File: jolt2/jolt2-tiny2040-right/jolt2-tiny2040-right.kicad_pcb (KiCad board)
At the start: 2 copper layers, 151 x 98 mm, 34 parts, among them J1 Conn_01x02_Pin, J10 Conn_01x02_Pin, J11 Conn_01x02_Pin, J12 Conn_01x02_Pin, J13 Conn_01x02_Pin, J14 Conn_01x02_Pin, J15 Conn_01x02_Pin, J16 Conn_01x02_Pin, J17 Conn_01x02_Pin, J18 Conn_01x02_Pin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

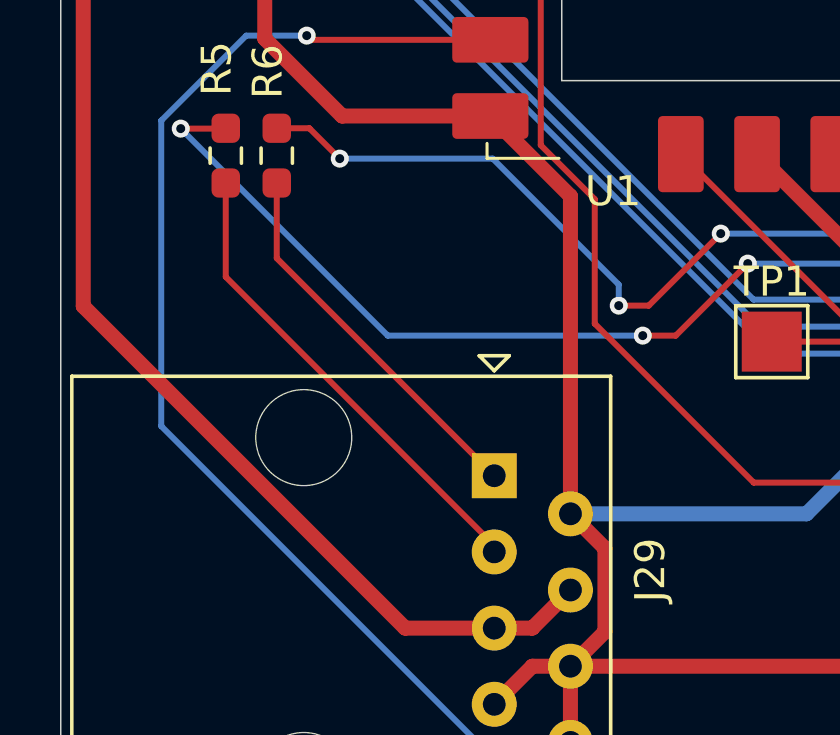
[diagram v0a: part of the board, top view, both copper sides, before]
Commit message: jolt2-tiny2040-right: Update PCB from schematic
Schematic was missing swapping TX and RX.
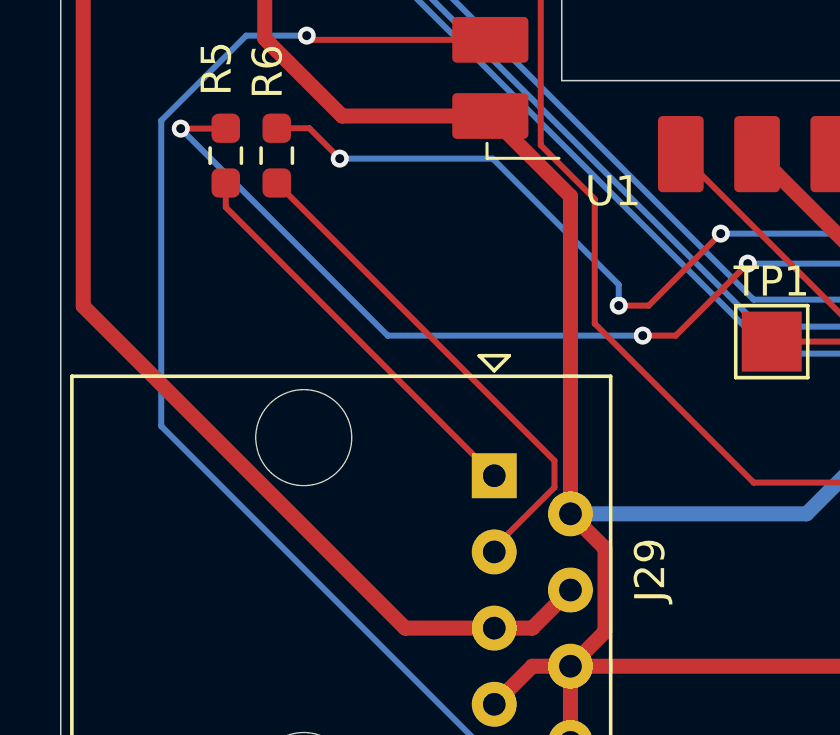
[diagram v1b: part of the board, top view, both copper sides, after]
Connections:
- J29 pad 1: SERRX -> SERTX
- J29 pad 3: SERTX -> SERRX
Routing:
- net SERRX: track 12.8 -> 17.2 mm
- net SERTX: track 16.0 -> 13.5 mm
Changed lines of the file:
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@@
 		)
 		(sheetname "Root")
-		(sheetfile "jolt2-tiny2040-left.kicad_sch")
+		(sheetfile "jolt2-tiny2040-right.kicad_sch")
 		(attr smd)
 		(fp_line
@@
 		(property ki_fp_filters "R_*")
 		(sheetname "Root")
-		(sheetfile "jolt2-tiny2040-left.kicad_sch")
+		(sheetfile "jolt2-tiny2040-right.kicad_sch")
 		(attr smd)
 		(fp_line
@@
 		(property ki_fp_filters "8P8C* RJ31* RJ32* RJ33* RJ34* RJ35* RJ41* RJ45* RJ49* RJ61*")
 		(sheetname "Root")
-		(sheetfile "jolt2-tiny2040-left.kicad_sch")
+		(sheetfile "jolt2-tiny2040-right.kicad_sch")
 		(attr through_hole)
 		(fp_line
@@
 			(layers "*.Cu" "*.Mask")
 			(remove_unused_layers no)
-			(net 11 "SERRX")
+			(net 12 "SERTX")
 			(pintype "passive")
 		)
@@
 			(layers "*.Cu" "*.Mask")
 			(remove_unused_layers no)
-			(net 12 "SERTX")
+			(net 11 "SERRX")
 			(pintype "passive")
 		)
@@
 		(property ki_fp_filters "Pin* Test*")
 		(sheetname "Root")
-		(sheetfile "jolt2-tiny2040-left.kicad_sch")
+		(sheetfile "jolt2-tiny2040-right.kicad_sch")
 		(attr exclude_from_pos_files)
 		(fp_line
@@
 		(property ki_fp_filters "R_*")
 		(sheetname "Root")
-		(sheetfile "jolt2-tiny2040-left.kicad_sch")
+		(sheetfile "jolt2-tiny2040-right.kicad_sch")
 		(attr smd)
 		(fp_line
@@
 	)
 	(segment
+		(start 28.45 136.565786)
+		(end 28.45 136.71)
+		(width 0.2)
+		(layer "F.Cu")
+		(net 11)
+	)
+	(segment
 		(start 21.2 124.4125)
-		(end 21.2 126.92)
+		(end 30.457893 133.670393)
 		(width 0.2)
 		(layer "F.Cu")
@@
 	)
 	(segment
-		(start 21.2 126.92)
-		(end 28.45 134.17)
+		(start 28.45 136.492284)
+		(end 28.45 136.71)
 		(width 0.2)
 		(layer "F.Cu")
@@
 	)
 	(segment
-		(start 19.5 124.4125)
-		(end 19.5 127.542284)
+		(start 30.457893 134.557893)
+		(end 28.45 136.565786)
 		(width 0.2)
 		(layer "F.Cu")
-		(net 12)
+		(net 11)
+	)
+	(segment
+		(start 30.457893 133.670393)
+		(end 30.457893 134.557893)
+		(width 0.2)
+		(layer "F.Cu")
+		(net 11)
 	)
 	(segment
-		(start 19.5 127.542284)
-		(end 28.45 136.492284)
+		(start 19.5 125.22)
+		(end 19.5 124.4125)
 		(width 0.2)
 		(layer "F.Cu")
@@
 	)
 	(segment
-		(start 28.45 136.492284)
-		(end 28.45 136.71)
+		(start 28.45 134.17)
+		(end 19.5 125.22)
 		(width 0.2)
 		(layer "F.Cu")
